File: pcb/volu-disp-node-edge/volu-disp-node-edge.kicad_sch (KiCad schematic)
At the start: 77 parts, among them J1 Conn_01x10_Socket, J10 Conn_01x03_Pin, J11 Conn_01x03_Pin, J12 Conn_01x03_Pin, J13 Conn_01x03_Pin, J14 Conn_01x03_Pin, J15 Conn_01x03_Pin, J16 Conn_01x03_Pin, J17 Conn_01x03_Pin, J18 Conn_01x03_Pin, J19 Conn_01x03_Pin, J2 Conn_01x03_Pin, J20 Conn_01x03_Pin, J21 Conn_01x03_Pin, J22 Conn_01x03_Pin, J23 Conn_01x03_Pin, J24 Conn_01x03_Pin, J25 Conn_01x03_Pin, J26 Conn_01x03_Pin, J27 Conn_01x03_Pin, J28 Conn_01x03_Pin, J29 Conn_01x03_Pin, J3 Conn_01x03_Pin, J30 Conn_01x03_Pin, J31 Conn_01x03_Pin, J32 Conn_01x03_Pin, J33 Conn_01x03_Pin, J4 Conn_01x03_Pin, J5 Conn_01x03_Pin, J6 Conn_01x03_Pin, J7 Conn_01x03_Pin, J8 Conn_01x03_Pin, J9 Conn_01x03_Pin, U1 74HCT595, U2 LMR51430, U3 74HCT595, U4 74HCT595, U5 74HCT595

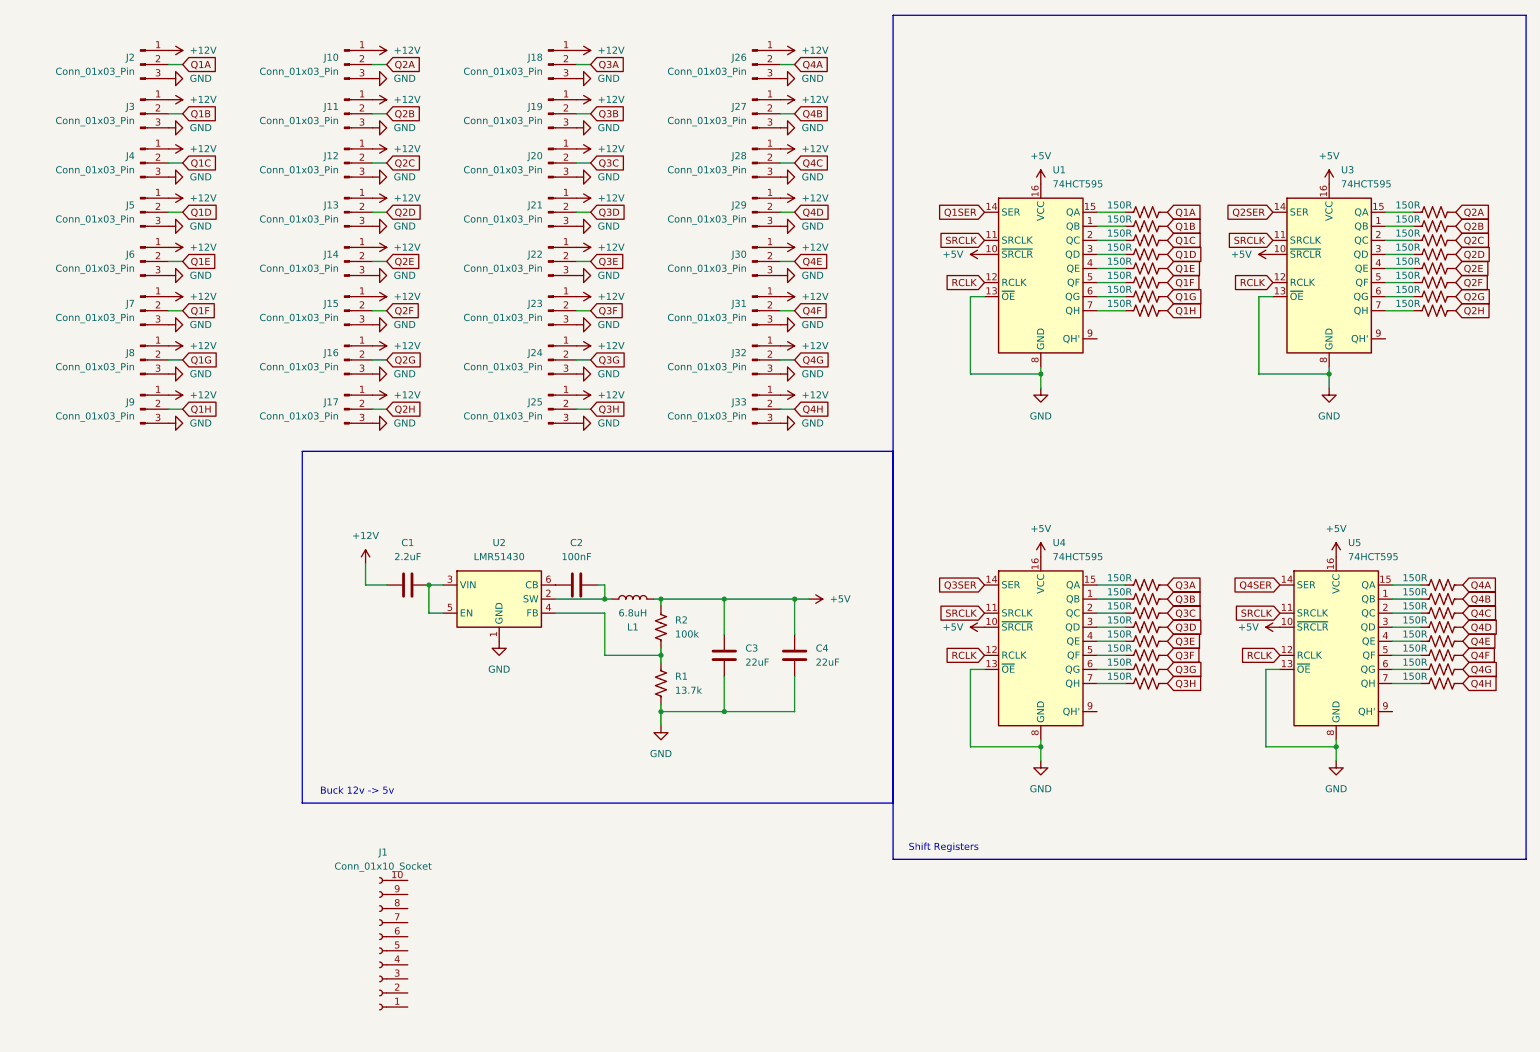
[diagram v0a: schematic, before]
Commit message: edge node schematic mostly done, need to add bulk caps still
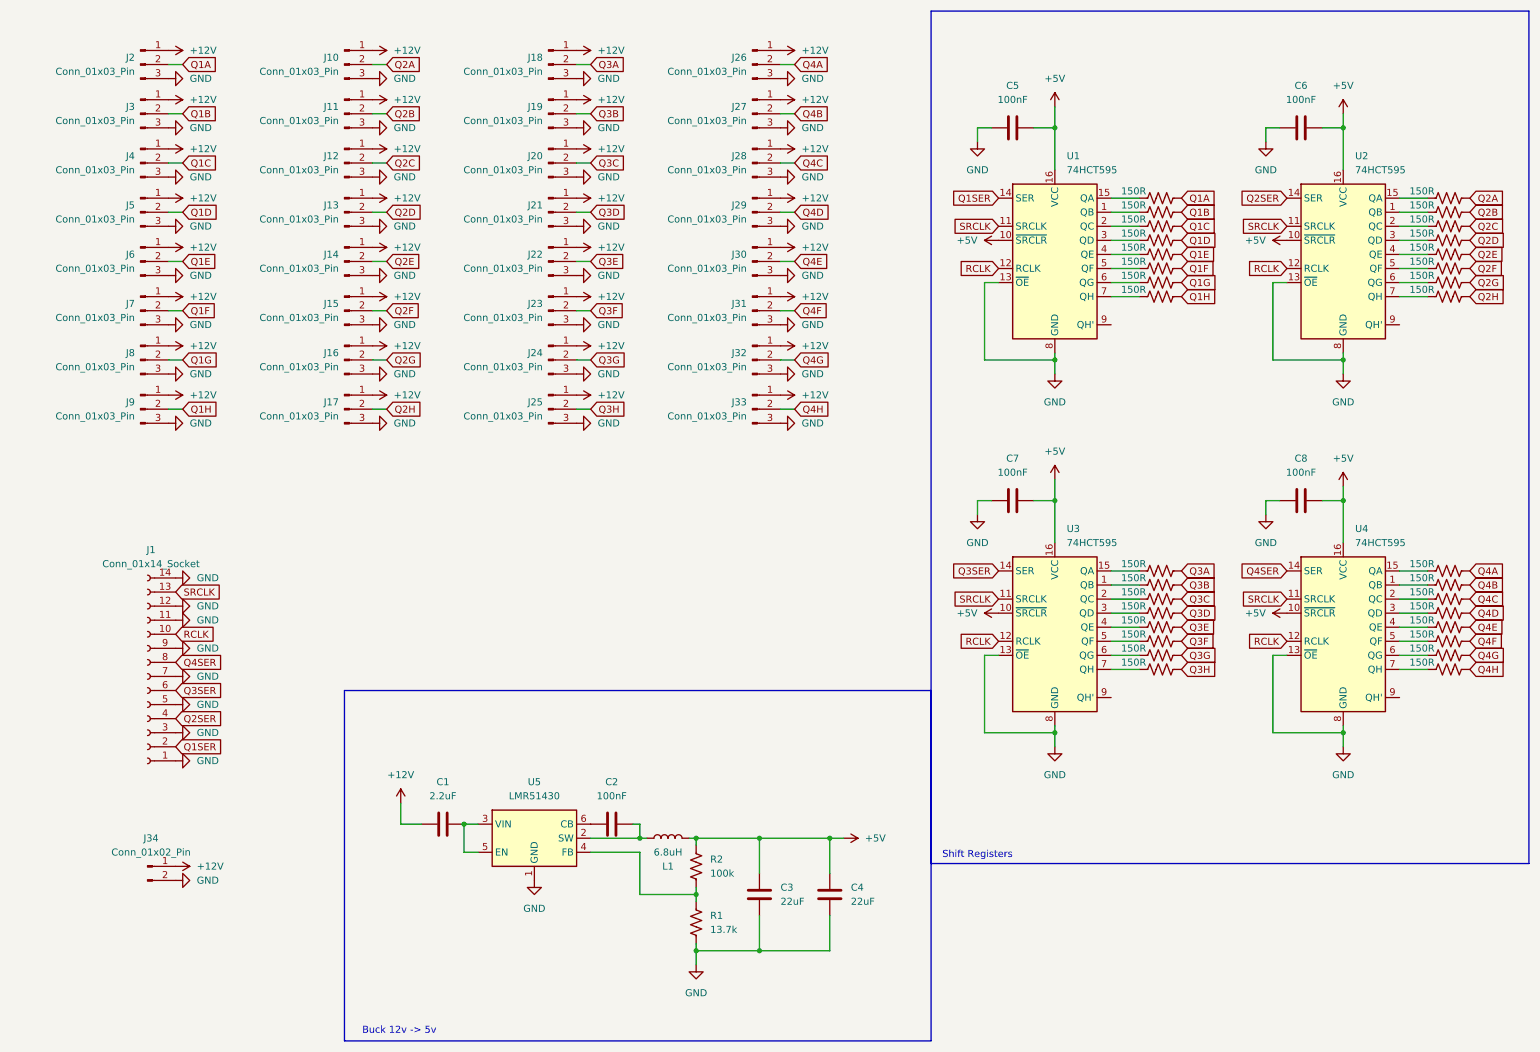
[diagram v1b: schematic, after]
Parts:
- removed J1: Conn_01x10_Socket, symbol Connector:Conn_01x10_Socket
- added C5, C6, C7, C8: 100nF, symbol Device:C
- added J1: Conn_01x14_Socket, symbol Connector:Conn_01x14_Socket
- added J34: Conn_01x02_Pin, symbol Connector:Conn_01x02_Pin
- renumbered U3 to U2, U4 to U3, U5 to U4, U2 to U5
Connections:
- net +12V: now also J34.1 (Pin_1)
- net +5V: now also C5.2, C6.2, C7.2, C8.2
- net GND: now also C5.1, C6.1, C7.1, C8.1, J1.1 (Pin_1), J1.11 (Pin_11), J1.12 (Pin_12), J1.14 (Pin_14), J1.3 (Pin_3), J1.5 (Pin_5), J1.7 (Pin_7), J1.9 (Pin_9), J34.2 (Pin_2)
- net Q1SER: now also J1.2 (Pin_2)
- net Q2SER: now also J1.4 (Pin_4)
- net Q3SER: now also J1.6 (Pin_6)
- net Q4SER: now also J1.8 (Pin_8)
- net RCLK: now also J1.10 (Pin_10)
- net SRCLK: now also J1.13 (Pin_13)
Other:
- moved on the sheet: C1, C2, C3, C4, L1, R1, R2, U1, U2, U3, U4, U5

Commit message: basic edge node schematic done, excludes fusing and soft-start
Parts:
- added C1, C2, C3, C4, C5, C6, C7, C8: 470uF, symbol Device:C
- J33: renamed from J1; value Conn_01x14_Socket -> 14-pin ribbon
- J34: value Conn_01x02_Pin -> XT-60
- renumbered C2 to C10, C3 to C11, C4 to C12, C5 to C13, C7 to C14, C6 to C15, C8 to C16, C1 to C9, J2 to J1, J11 to J10, J12 to J11, J13 to J12, J14 to J13, J15 to J14, J16 to J15, J17 to J16, J18 to J17, J19 to J18, J20 to J19, J3 to J2, J21 to J20, J22 to J21, J23 to J22, J24 to J23, J25 to J24, J26 to J25, J27 to J26, J28 to J27, J29 to J28, J30 to J29, J4 to J3, J31 to J30, J32 to J31, J33 to J32, J5 to J4, J6 to J5, J7 to J6, J8 to J7, J9 to J8, J10 to J9, R2 to R1, R3 to R10, R19 to R11, R20 to R12, R21 to R13, R22 to R14, R23 to R15, R24 to R16, R25 to R17, R26 to R18, R11 to R19, R1 to R2, R12 to R20, R13 to R21, R14 to R22, R15 to R23, R16 to R24, R17 to R25, R18 to R26, R10 to R3, R9 to R4, R8 to R5, R7 to R6, R6 to R7, R5 to R8, R4 to R9
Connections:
- net +12V: now also C1.1, C2.1, C3.1, C4.1, C5.1, C6.1, C7.1, C8.1
- net GND: now also C1.2, C2.2, C3.2, C4.2, C5.2, C6.2, C7.2, C8.2
- no-connect marks 0 -> 4
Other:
- note added: "12V Rail Bulk Capacitance"
- note added: "Input Connectors"
- note added: "Output Connectors"
- moved on the sheet: J1, J10, J11, J12, J13, J14, J15, J16, J17, J18, J19, J2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

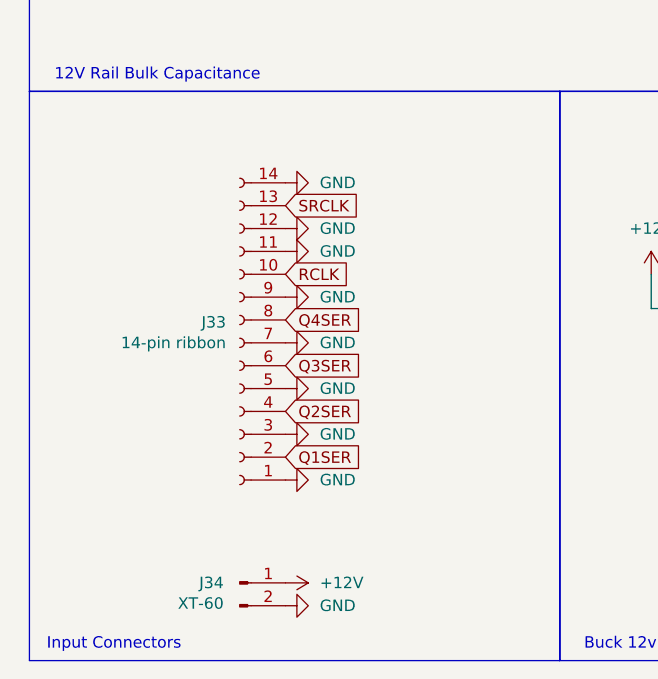
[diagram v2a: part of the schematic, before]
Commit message: assigned footprints
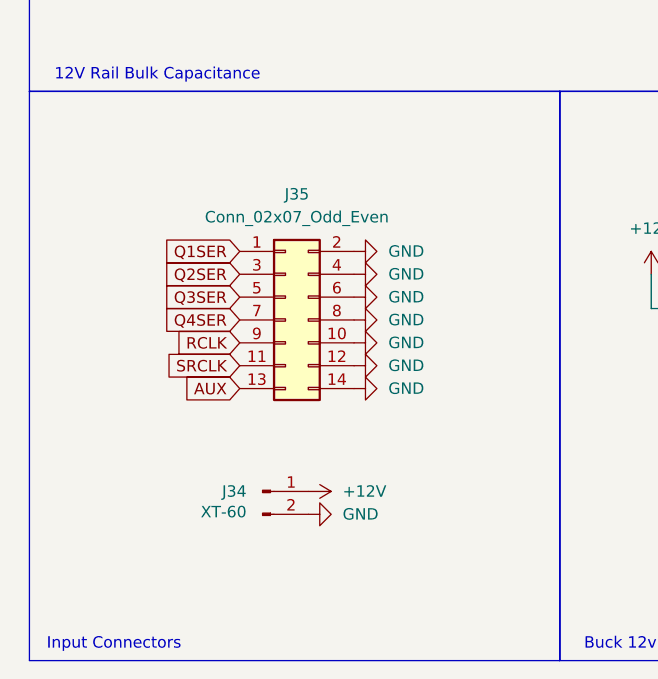
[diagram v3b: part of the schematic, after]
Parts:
- removed J33: 14-pin ribbon, symbol Connector:Conn_01x14_Socket
- added J35: Conn_02x07_Odd_Even, Connector_IDC:IDC-Header_2x07_P2.54mm_Latch_Vertical, symbol Connector_Generic:Conn_02x07_Odd_Even
- C1, C2, C3, C4, C5, C6, C7, C8: footprint (none) -> Capacitor_THT:CP_Radial_D10.0mm_P5.00mm
- C10, C11, C12, C13, C14, C15, C16, C9: footprint (none) -> Capacitor_SMD:C_0805_2012Metric
- J1, J10, J11, J12, J13, J14, J15, J16, J17, J18, J19, J2, J20, J21, J22, J23, J24, J25, J26, J27, J28, J29, J3, J30, J31, J32, J4, J5, J6, J7, J8, J9: footprint (none) -> Connector_JST:JST_XH_B3B-XH-A_1x03_P2.50mm_Vertical
- J34, L1, R1, R10, R11, R12, R13, R14, R15, R16, R17, R18, R19, R2, R20, R21, R22, R23, R24, R25, R26, R27, R28, R29, R3, R30, R31, R32, R33, R34, R4, R5, R6, R7, R8, R9: footprint (none) -> Resistor_SMD:R_0603_1608Metric
- U1, U2, U3, U4: footprint (none) -> Package_SO:SOIC-16_3.9x9.9mm_P1.27mm
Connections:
- net GND: now also J35.10 (Pin_10), J35.12 (Pin_12), J35.14 (Pin_14), J35.2 (Pin_2), J35.4 (Pin_4), J35.6 (Pin_6), J35.8 (Pin_8)
- net Q1SER: now also J35.1 (Pin_1)
- net Q2SER: now also J35.3 (Pin_3)
- net Q3SER: now also J35.5 (Pin_5)
- net Q4SER: now also J35.7 (Pin_7)
- net RCLK: now also J35.9 (Pin_9)
- net SRCLK: now also J35.11 (Pin_11)
- new net AUX: J35.13 (Pin_13)
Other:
- moved on the sheet: J34

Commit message: edge node schematic done, pcb done. next is main node circuit and pcb
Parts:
- removed C1, C2, C3, C4, C5, C6, C7, C8: 470uF, Capacitor_THT:CP_Radial_D10.0mm_P5.00mm, symbol Device:C
- removed R10, R11, R12, R13, R14, R15, R16, R17, R18, R19, R20, R21, R22, R23, R24, R25, R26, R27, R28, R29, R3, R30, R31, R32, R33, R34, R4, R5, R6, R7, R8, R9: 150R, Resistor_SMD:R_0603_1608Metric, symbol Device:R_US
- added H1, H2, H3, H4: MountingHole, MountingHole:MountingHole_4.3mm_M4, symbol Mechanical:MountingHole
- added Q2: NMOS, Package_TO_SOT_SMD:SOT-23, symbol Simulation_SPICE:NMOS
- added R42: 10k, Resistor_SMD:R_0603_1608Metric, symbol Device:R_US
- added RN1, RN2, RN3, RN4, RN5, RN6, RN7, RN8: 150R, Resistor_SMD:R_Array_Convex_4x0603, symbol Device:R_Pack04
- C10, C13, C14, C15, C16, C9: footprint Capacitor_SMD:C_0805_2012Metric -> Capacitor_SMD:C_0603_1608Metric
- J34: footprint Resistor_SMD:R_0603_1608Metric -> Connector_AMASS:AMASS_XT60PW-M_1x02_P7.20mm_Horizontal
- L1: footprint Resistor_SMD:R_0603_1608Metric -> Inductor_SMD:L_7.3x7.3_H3.5
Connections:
- net +5V: now also Q2.2 (G), R42.1
- net GND: now also C9.2, Q2.3 (S), R42.2; no longer J35.14 (Pin_14)
- net Q1A: now also RN5.5 (R4.2)
- net Q1B: now also RN5.6 (R3.2)
- net Q1C: now also RN5.7 (R2.2)
- net Q1D: now also RN5.8 (R1.2)
- net Q1E: now also RN6.5 (R4.2)
- net Q1F: now also RN6.6 (R3.2)
- net Q1G: now also RN6.7 (R2.2)
- net Q1H: now also RN6.8 (R1.2)
- net Q2A: now also RN7.5 (R4.2)
- net Q2B: now also RN7.6 (R3.2)
- net Q2C: now also RN7.7 (R2.2)
- net Q2D: now also RN7.8 (R1.2)
- net Q2E: now also RN8.5 (R4.2)
- net Q2F: now also RN8.6 (R3.2)
- net Q2G: now also RN8.7 (R2.2)
- net Q2H: now also RN8.8 (R1.2)
- net Q3A: now also RN2.5 (R4.2)
- net Q3B: now also RN2.6 (R3.2)
- net Q3C: now also RN2.7 (R2.2)
- net Q3D: now also RN2.8 (R1.2)
- net Q3E: now also RN1.5 (R4.2)
- net Q3F: now also RN1.6 (R3.2)
- net Q3G: now also RN1.7 (R2.2)
- net Q3H: now also RN1.8 (R1.2)
- net Q4A: now also RN3.5 (R4.2)
- net Q4B: now also RN3.6 (R3.2)
- net Q4C: now also RN3.7 (R2.2)
- net Q4D: now also RN3.8 (R1.2)
- net Q4E: now also RN4.5 (R4.2)
- net Q4F: now also RN4.6 (R3.2)
- net Q4G: now also RN4.7 (R2.2)
- net Q4H: now also RN4.8 (R1.2)
- net at U1.5 (QF): now also RN6.3 (R3.1)
- net at U2.1 (QB): now also RN7.3 (R3.1)
- net at U4.6 (QG): now also RN4.2 (R2.1)
- net at U2.2 (QC): now also RN7.2 (R2.1)
- net at U1.1 (QB): now also RN5.3 (R3.1)
- net at U4.3 (QD): now also RN3.1 (R1.1)
- net at U4.2 (QC): now also RN3.2 (R2.1)
- net at U4.4 (QE): now also RN4.4 (R4.1)
- net at U1.7 (QH): now also RN6.1 (R1.1)
- net at U2.3 (QD): now also RN7.1 (R1.1)
- net at U3.7 (QH): now also RN1.1 (R1.1)
- net at U1.15 (QA): now also RN5.4 (R4.1)
- net at U3.6 (QG): now also RN1.2 (R2.1)
- net at U3.15 (QA): now also RN2.4 (R4.1)
- net at U4.7 (QH): now also RN4.1 (R1.1)
- net at U1.2 (QC): now also RN5.2 (R2.1)
- net at U1.3 (QD): now also RN5.1 (R1.1)
- net at U1.4 (QE): now also RN6.4 (R4.1)
- net at U1.6 (QG): now also RN6.2 (R2.1)
- net at U4.1 (QB): now also RN3.3 (R3.1)
- net at U3.1 (QB): now also RN2.3 (R3.1)
- net at U4.15 (QA): now also RN3.4 (R4.1)
- net at U4.5 (QF): now also RN4.3 (R3.1)
- net at U3.3 (QD): now also RN2.1 (R1.1)
- net at U2.15 (QA): now also RN7.4 (R4.1)
- net at U2.5 (QF): now also RN8.3 (R3.1)
- net +12V_SW: now reaches C9.1, U5.3 (VIN), U5.5 (EN)
- net +12V_SW: now also J1.1 (Pin_1), J10.1 (Pin_1), J11.1 (Pin_1), J12.1 (Pin_1), J13.1 (Pin_1), J14.1 (Pin_1), J15.1 (Pin_1), J16.1 (Pin_1), J17.1 (Pin_1), J18.1 (Pin_1), J19.1 (Pin_1), J2.1 (Pin_1), J20.1 (Pin_1), J21.1 (Pin_1), J22.1 (Pin_1), J23.1 (Pin_1), J24.1 (Pin_1), J25.1 (Pin_1), J26.1 (Pin_1), J27.1 (Pin_1), J28.1 (Pin_1), J29.1 (Pin_1), J3.1 (Pin_1), J30.1 (Pin_1), J31.1 (Pin_1), J32.1 (Pin_1), J4.1 (Pin_1), J5.1 (Pin_1), J6.1 (Pin_1), J7.1 (Pin_1), J8.1 (Pin_1), J9.1 (Pin_1)
- net at U2.4 (QE): now also RN8.4 (R4.1)
- net at U2.6 (QG): now also RN8.2 (R2.1)
- net at U2.7 (QH): now also RN8.1 (R1.1)
- net at U3.5 (QF): now also RN1.3 (R3.1)
- net at U3.4 (QE): now also RN1.4 (R4.1)
- net at U3.2 (QC): now also RN2.2 (R2.1)
- removed net +12V: C9.2, J1.1 (Pin_1), J10.1 (Pin_1), J11.1 (Pin_1), J12.1 (Pin_1), J13.1 (Pin_1), J14.1 (Pin_1), J15.1 (Pin_1), J16.1 (Pin_1), J17.1 (Pin_1), J18.1 (Pin_1), J19.1 (Pin_1), J2.1 (Pin_1), J20.1 (Pin_1), J21.1 (Pin_1), J22.1 (Pin_1), J23.1 (Pin_1), J24.1 (Pin_1), J25.1 (Pin_1), J26.1 (Pin_1), J27.1 (Pin_1), J28.1 (Pin_1), J29.1 (Pin_1), J3.1 (Pin_1), J30.1 (Pin_1), J31.1 (Pin_1), J32.1 (Pin_1), J34.1 (Pin_1), J4.1 (Pin_1), J5.1 (Pin_1), J6.1 (Pin_1), J7.1 (Pin_1), J8.1 (Pin_1), J9.1 (Pin_1)
- net AUX renamed PWR_GOOD
- new net +12V_IN: J34.1 (Pin_1)
- new net 5V_PRESENT: J35.14 (Pin_14), Q2.1 (D)
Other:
- added sheet Hot Swap Control (hot_swap_control.kicad_sch)
- note added: "5V Detecting"
- note added: "Hot Swap Controller"
- note added: "Strip Output Connectors"
- note removed: "12V Rail Bulk Capacitance"
- note removed: "Output Connectors"
- moved on the sheet: C9
